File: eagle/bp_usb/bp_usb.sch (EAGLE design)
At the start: 2 parts

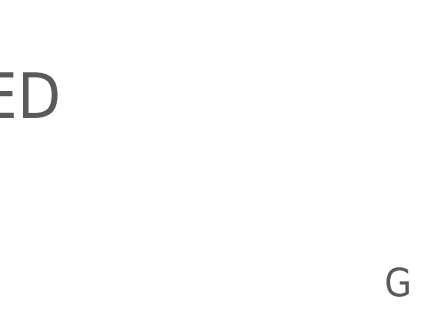
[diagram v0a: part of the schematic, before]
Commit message: Modified USB back panel to move GPI/O cutout and fixed schematic file name.
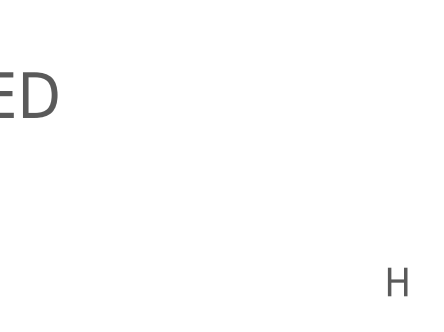
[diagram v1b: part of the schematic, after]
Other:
- note added: "H"
- note removed: "G"
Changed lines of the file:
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@@
 <?xml version="1.0" encoding="utf-8"?>
 <!DOCTYPE eagle SYSTEM "eagle.dtd">
-<eagle version="9.3.2">
+<eagle version="9.4.0">
 <drawing>
 <settings>
@@
 <plain>
 <text x="177.8" y="26.162" size="5.08" layer="97">Back Panel - LED</text>
-<text x="266.7" y="6.35" size="3.175" layer="97">G</text>
+<text x="266.7" y="6.35" size="3.175" layer="97">H</text>
 </plain>
 <instances>

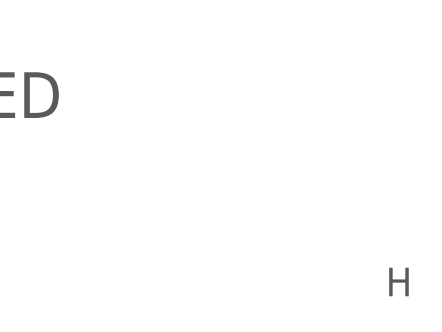
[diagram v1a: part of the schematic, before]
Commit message: Added brief fab notes to back panel PCB design.
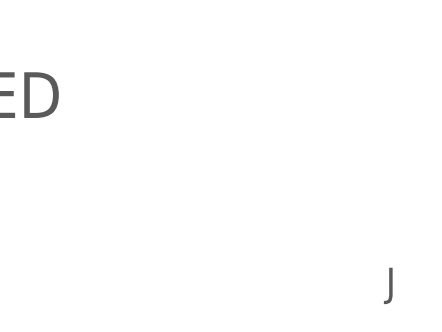
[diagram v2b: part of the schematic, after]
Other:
- note added: "J"
- note removed: "H"
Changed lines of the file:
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@@
 <?xml version="1.0" encoding="utf-8"?>
 <!DOCTYPE eagle SYSTEM "eagle.dtd">
-<eagle version="9.4.0">
+<eagle version="9.5.0">
 <drawing>
 <settings>
@@
 <plain>
 <text x="177.8" y="26.162" size="5.08" layer="97">Back Panel - LED</text>
-<text x="266.7" y="6.35" size="3.175" layer="97">H</text>
+<text x="266.7" y="6.35" size="3.175" layer="97">J</text>
 </plain>
 <instances>
